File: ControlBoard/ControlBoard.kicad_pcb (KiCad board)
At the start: 2 copper layers, 82.5 x 60.1 mm, 24 parts, among them CON1 BARREL_JACK, J1 OrangePiPrime, J2 CONN_01X10, J3 CONN_02X10, J4 RJ45, J5 CONN_02X03, J6 RF_TX, J7 RF_RX, M1 DC-DC_REG, SW1 SW_Push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

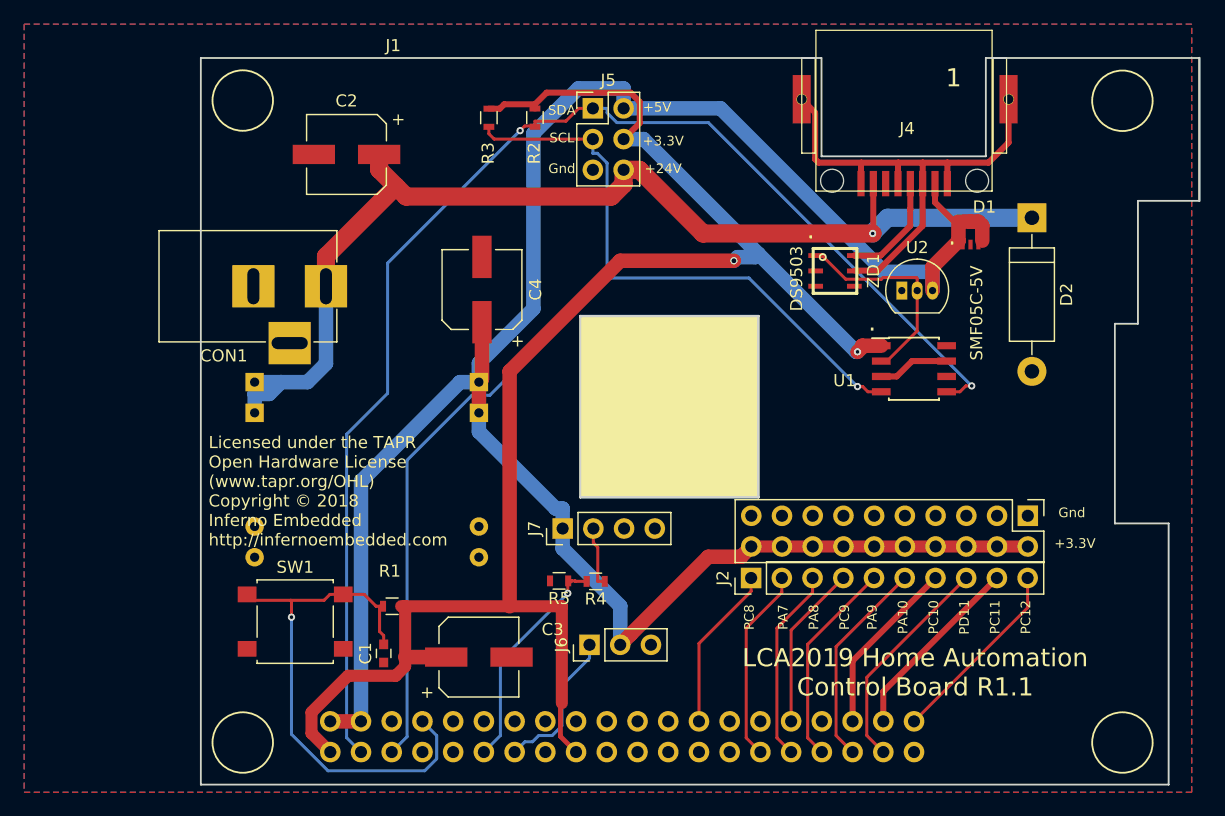
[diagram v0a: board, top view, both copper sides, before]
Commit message: Revision 1.2 of the Control Board - All resisitors to 10k - Add solder jumpers to set i2c address - Move the GPIO +V line to 3.3V - Move pushbutton to PA6 as it has an interrupt associated with it - Update copyright year - Add OSHW & Inferno Embedded logos that was lost - Use SMD 28V zener for ESD protection on the 28V line - Use SMD 5.1V zener for ESD protection on the 5V line - Add a 2A polyswitch (fuse) to protect against overcurrent through the PSU - Switch the dc-dc footprint to SMD pads - Switch from electrolytic to ceramic caps (cheaper, easier to install) - Add a cutout for access to the serial header
Signed-off-by: Alastair D'Silva <alastair@d-silva.org>
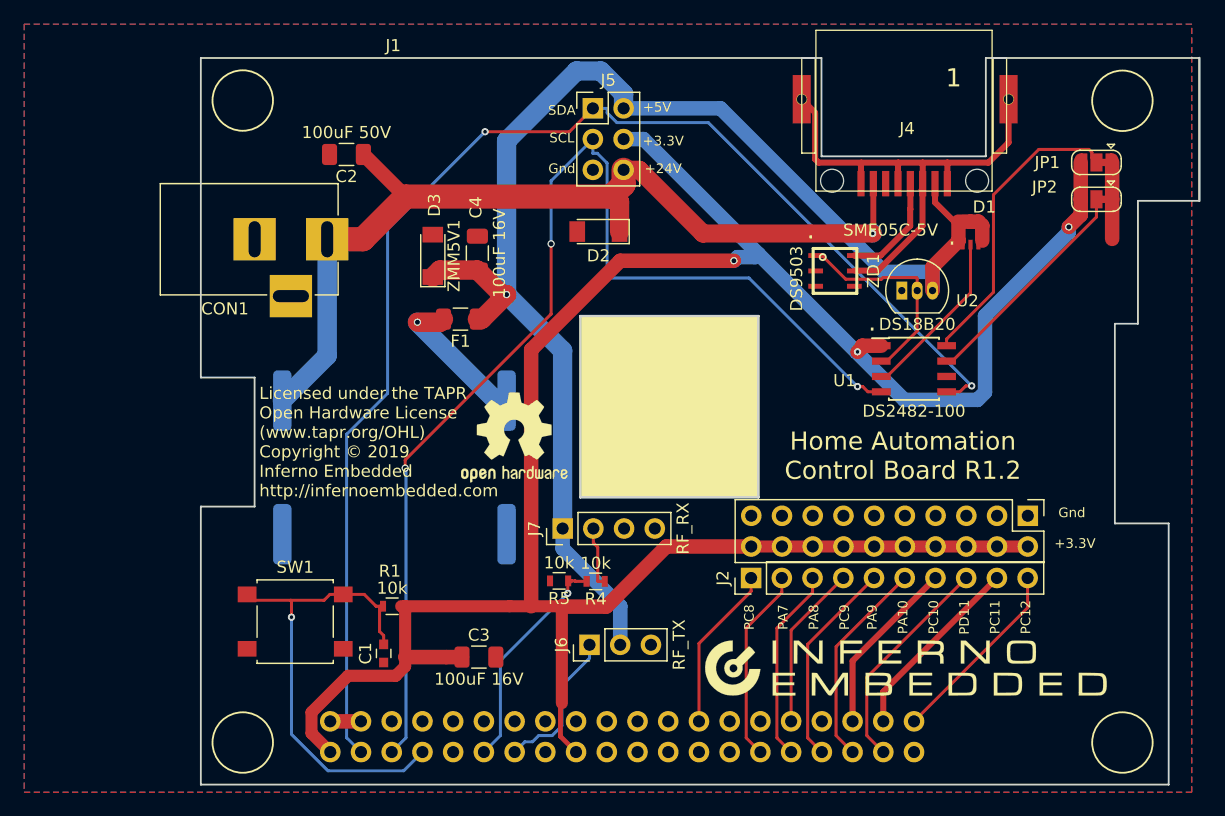
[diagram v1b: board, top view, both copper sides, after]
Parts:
- removed R2, R3: 4.7k, Resistors_SMD:R_0603
- added D3: ZMM5V1, Diode_SMD:D_MiniMELF, F.Cu at (89.7, 62.3)
- added F1: Polyfuse, Fuse:Fuse_1206_3216Metric, F.Cu at (91.9, 67.6)
- added G***: LOGO, InfernoEmbedded:inferno_embedded_6mm, F.Cu at (128.8, 96.4)
- added JP1: SolderJumper_3_Bridged12, Jumper:SolderJumper-3_P1.3mm_Bridged12_RoundedPad1.0x1.5mm, F.Cu at (144.5, 54.6)
- added JP2: SolderJumper_3_Bridged12, Jumper:SolderJumper-3_P1.3mm_Bridged12_RoundedPad1.0x1.5mm, F.Cu at (144.5, 57.7)
- added REF**: OSHW-Logo2_9.8x8mm_SilkScreen, Symbol:OSHW-Logo2_9.8x8mm_SilkScreen, F.Cu at (96.4, 77.3)
- C2: value 100uF -> 100uF 50V; footprint Capacitors_SMD:CP_Elec_6.3x7.7 -> Capacitor_SMD:C_1206_3216Metric
- C3, C4: value 100uF -> 100uF 16V; footprint Capacitors_SMD:CP_Elec_6.3x7.7 -> Capacitor_SMD:C_1206_3216Metric
- D2: value P6KE24A -> ZMM24V; footprint Diodes_ThroughHole:D_DO-15_P12.70mm_Horizontal -> Diode_SMD:D_MiniMELF
- M1: footprint D-Sun DC-DC Regulator:D-SUN_DC_DC -> DC-DC:D-SUN_DC_DC
- R5: value 16k -> 10k
- moved D2 35.9 mm to (103.3, 60.3), turned to 180 degrees
- moved CON1 3.89 mm to (80.9, 61.0)
- moved C4 3.04 mm to (93.3, 62.1)
- moved M1 2.29 mm to (75.4, 71.5)
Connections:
- J1 pad 7: Net-(J1-Pad7) -> Net-(C1-Pad2)
- J1 pad 8: Net-(C1-Pad2) -> Net-(J1-Pad8)
- J3 pad 10: +5V -> +3V3
- J3 pad 12: +5V -> +3V3
- J3 pad 14: +5V -> +3V3
- J3 pad 16: +5V -> +3V3
- J3 pad 18: +5V -> +3V3
- J3 pad 2: +5V -> +3V3
- J3 pad 20: +5V -> +3V3
- J3 pad 4: +5V -> +3V3
- J3 pad 6: +5V -> +3V3
- J3 pad 8: +5V -> +3V3
- M1 pad 3: +5V -> Net-(F1-Pad2)
- U1 pad 7: GND -> Net-(JP2-Pad2)
- U1 pad 8: GND -> Net-(JP1-Pad2)
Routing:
- net +5V: track 185.3 -> 120.3 mm, vias 0 -> 1
- net +3V3: track 138.0 -> 196.7 mm, vias 2 -> 3
- net Net-(JP1-Pad2): track 0.00 -> 24.9 mm
- net Net-(JP2-Pad2): track 0.00 -> 18.8 mm
- net +24V: track 92.9 -> 78.2 mm
- net GND: track 5.93 -> 20.6 mm
- net Net-(F1-Pad2): track 0.00 -> 12.3 mm, vias 0 -> 1
- net Net-(C1-Pad2): track 44.0 -> 39.4 mm
- net /SDA: track 108.2 -> 109.5 mm
- net /SCL: track 95.5 -> 96.4 mm, vias 1 -> 3
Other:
- outline, holes or cut-outs redrawn
- net class High Power: trace_width 1.2 -> 1.6
- board text added: "Home Automation Control Board R1.2"
- board text added: "Licensed under the TAPR Open Hardware License (www.tapr.org/OHL) Copyright © 2019 Inferno Embedded http://infernoembedded.com"
- board text removed: "LCA2019 Home Automation Control Board R1.1"
- board text removed: "Licensed under the TAPR Open Hardware License (www.tapr.org/OHL) Copyright © 2018 Inferno Embedded http://infernoembedded.com"

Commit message: Controlboard updates - Add second I2C port - Add Power LEDs (5V & 3.3V) - Add GPIO LED on PA2 - Add header for ST7735 LCD - Add missing mounting holes - Save OrangePiPrime footprints and symbols as explicit libs
Signed-off-by: Alastair D'Silva <alastair@d-silva.org>
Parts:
- added D4: LED, LED_SMD:LED_0603_1608Metric, F.Cu at (118.0, 56.0)
- added D5: LED, LED_SMD:LED_0603_1608Metric, F.Cu at (115.8, 56.0)
- added D6: LED, LED_SMD:LED_0603_1608Metric, F.Cu at (112.3, 88.9)
- added J10: Conn_01x08_Female, Connector_PinSocket_2.54mm:PinSocket_1x08_P2.54mm_Vertical, F.Cu at (141.5, 57.4)
- added J8: CONN_02X03, Connector_PinHeader_2.54mm:PinHeader_2x03_P2.54mm_Vertical, F.Cu at (88.6, 50.2)
- added R2: 169R, Resistor_SMD:R_0603_1608Metric, F.Cu at (112.9, 49.4)
- added R3: 10R, Resistor_SMD:R_0603_1608Metric, F.Cu at (112.9, 52.7)
- added R6: 10R, Resistor_SMD:R_0603_1608Metric, F.Cu at (112.3, 92.2)
- added REF**: MountingHole_3.2mm_M3, MountingHole:MountingHole_3.2mm_M3, F.Cu at (146.7, 49.5)
- added REF**: MountingHole_3.2mm_M3, MountingHole:MountingHole_3.2mm_M3, F.Cu at (146.7, 102.6)
- added REF**: MountingHole_3.2mm_M3, MountingHole:MountingHole_3.2mm_M3, F.Cu at (73.9, 102.6)
- added REF**: MountingHole_3.2mm_M3, MountingHole:MountingHole_3.2mm_M3, F.Cu at (73.9, 49.5)
- D2: value ZMM24V -> ZMM27V
- J1: value OrangePiPrime -> OrangePi_OrangePiPrime; footprint OrangePi:OrangePiPrime -> OrangePiPrime:OrangePiPrime
- J2: footprint Pin_Headers:Pin_Header_Straight_1x10_Pitch2.54mm -> Connector_PinHeader_2.54mm:PinHeader_1x10_P2.54mm_Vertical
- J3: footprint Pin_Headers:Pin_Header_Straight_2x10_Pitch2.54mm -> Connector_PinHeader_2.54mm:PinHeader_2x10_P2.54mm_Vertical
- J5: footprint Pin_Headers:Pin_Header_Straight_2x03_Pitch2.54mm -> Connector_PinHeader_2.54mm:PinHeader_2x03_P2.54mm_Vertical
- J6: footprint Pin_Headers:Pin_Header_Straight_1x03_Pitch2.54mm -> Connector_PinHeader_2.54mm:PinHeader_1x03_P2.54mm_Vertical
- J7: footprint Pin_Headers:Pin_Header_Straight_1x04_Pitch2.54mm -> Connector_PinHeader_2.54mm:PinHeader_1x04_P2.54mm_Vertical
- moved C3 19.1 mm to (112.5, 95.9), turned to 180 degrees
- moved JP2 15.9 mm to (136.6, 71.5)
- moved JP1 15.8 mm to (136.6, 68.3)
- moved C2 8.87 mm to (85.7, 62.2), turned to 270 degrees
- moved U1 4.74 mm to (124.7, 72.0)
- moved G*** 3.30 mm to (132.1, 96.5)
- moved REF** 0.38 mm to (96.8, 77.3)
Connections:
- J1 pad 10: Net-(J1-Pad10) -> /DISPLAY_BACKLIGHT
- J1 pad 16: Net-(J1-Pad16) -> /DISPLAY_RESET
- J1 pad 18: Net-(J1-Pad18) -> /DISPLAY_DC
- J1 pad 23: (no net) -> Net-(J1-Pad23)
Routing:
- net GND: track 20.6 -> 416.0 mm, vias 0 -> 3
- net +3V3: track 196.7 -> 281.1 mm, vias 3 -> 2
- net /DISPLAY_BACKLIGHT: track 0.00 -> 79.4 mm, vias 0 -> 1
- net /SDA2: track 0.00 -> 77.4 mm, vias 0 -> 2
- net /SCL2: track 0.00 -> 71.9 mm, vias 0 -> 2
- net Net-(J1-Pad19): track 0.00 -> 69.5 mm, vias 0 -> 1
- net /DISPLAY_DC: track 0.00 -> 59.2 mm
- net Net-(J1-Pad23): track 0.00 -> 58.9 mm, vias 0 -> 1
- net /DISPLAY_RESET: track 0.00 -> 58.2 mm
- net +5V: track 120.3 -> 176.1 mm, vias 1 -> 0
- net Net-(J1-Pad24): track 0.00 -> 49.3 mm
- net /SDA: track 109.5 -> 92.5 mm, vias 2 -> 3
- net Net-(JP1-Pad2): track 24.9 -> 10.5 mm
- net Net-(J1-Pad22): track 0.00 -> 10.6 mm, vias 0 -> 1
- net Net-(JP2-Pad2): track 18.8 -> 10.6 mm
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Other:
- net class High Power: trace_width 1.6 -> 2
- net class Power: trace_width 1.2 -> 0.8
- board text added: "PA2"
- board text added: "SCL0"
- board text added: "SCL1"
- board text added: "SDA0"
- board text added: "SDA1"
- board text removed: "SCL"
- board text removed: "SDA"
